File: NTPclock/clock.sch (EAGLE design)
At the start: 27 parts, among them IC1 MAX7219CNG

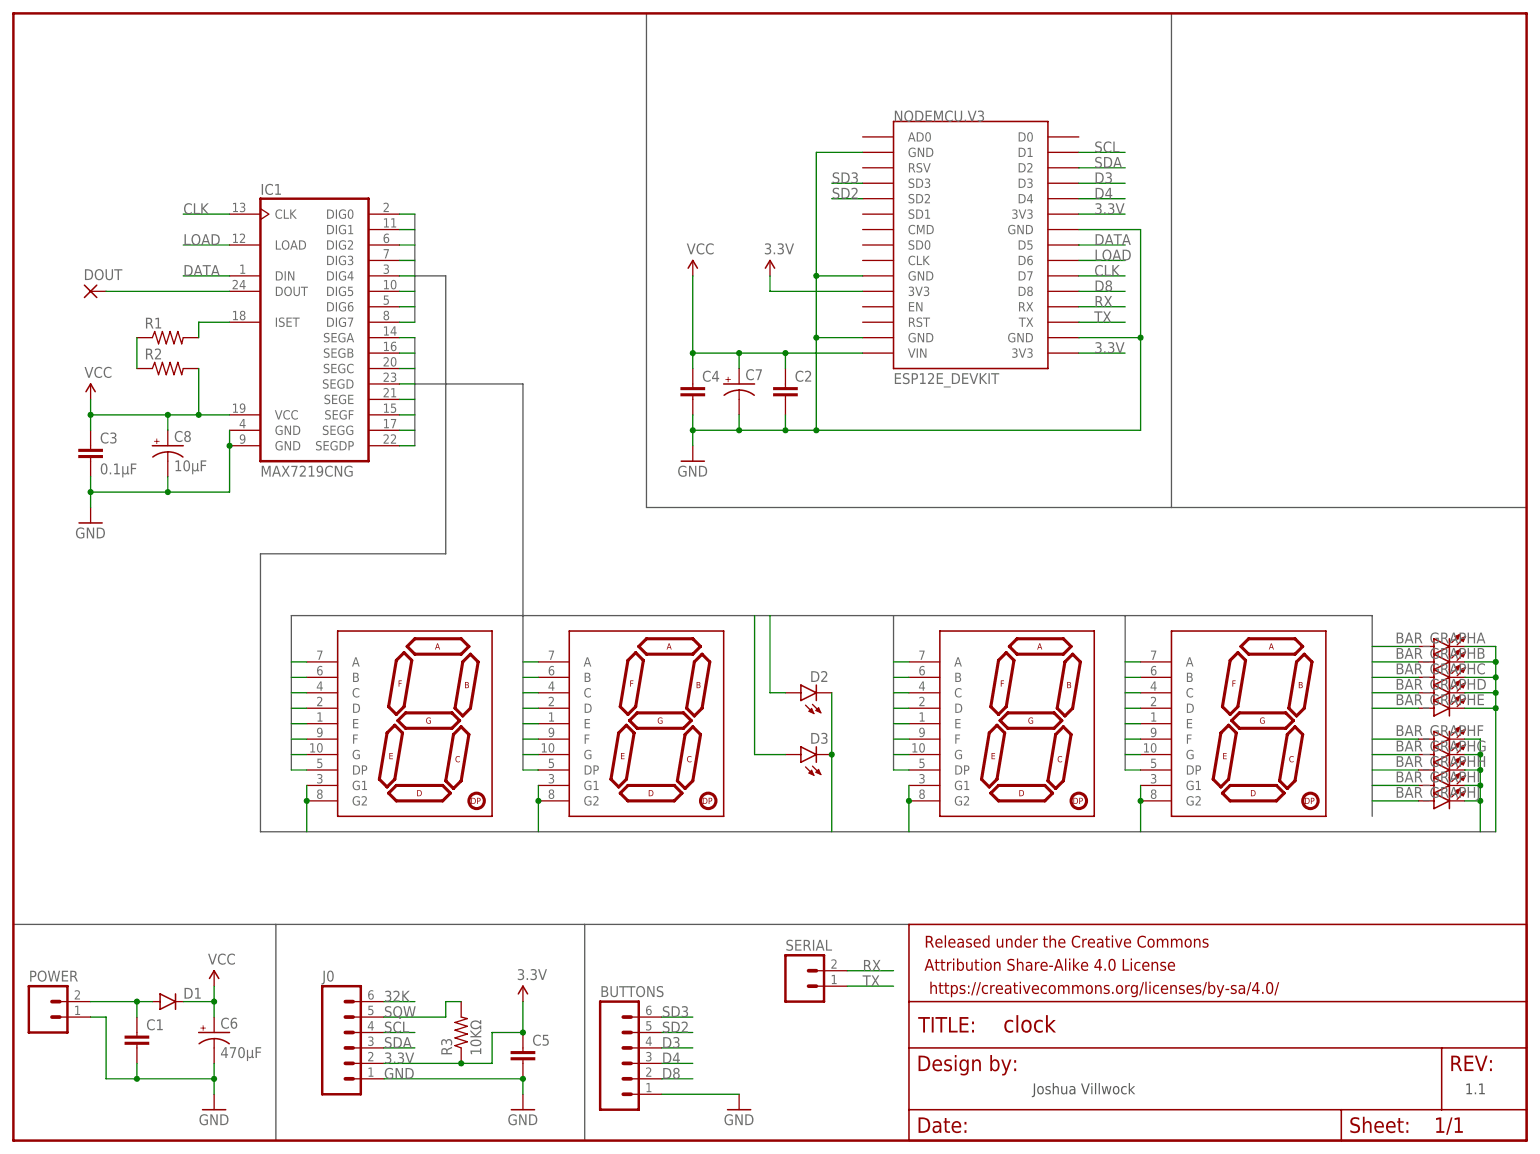
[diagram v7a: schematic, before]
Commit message: Added capacitor values
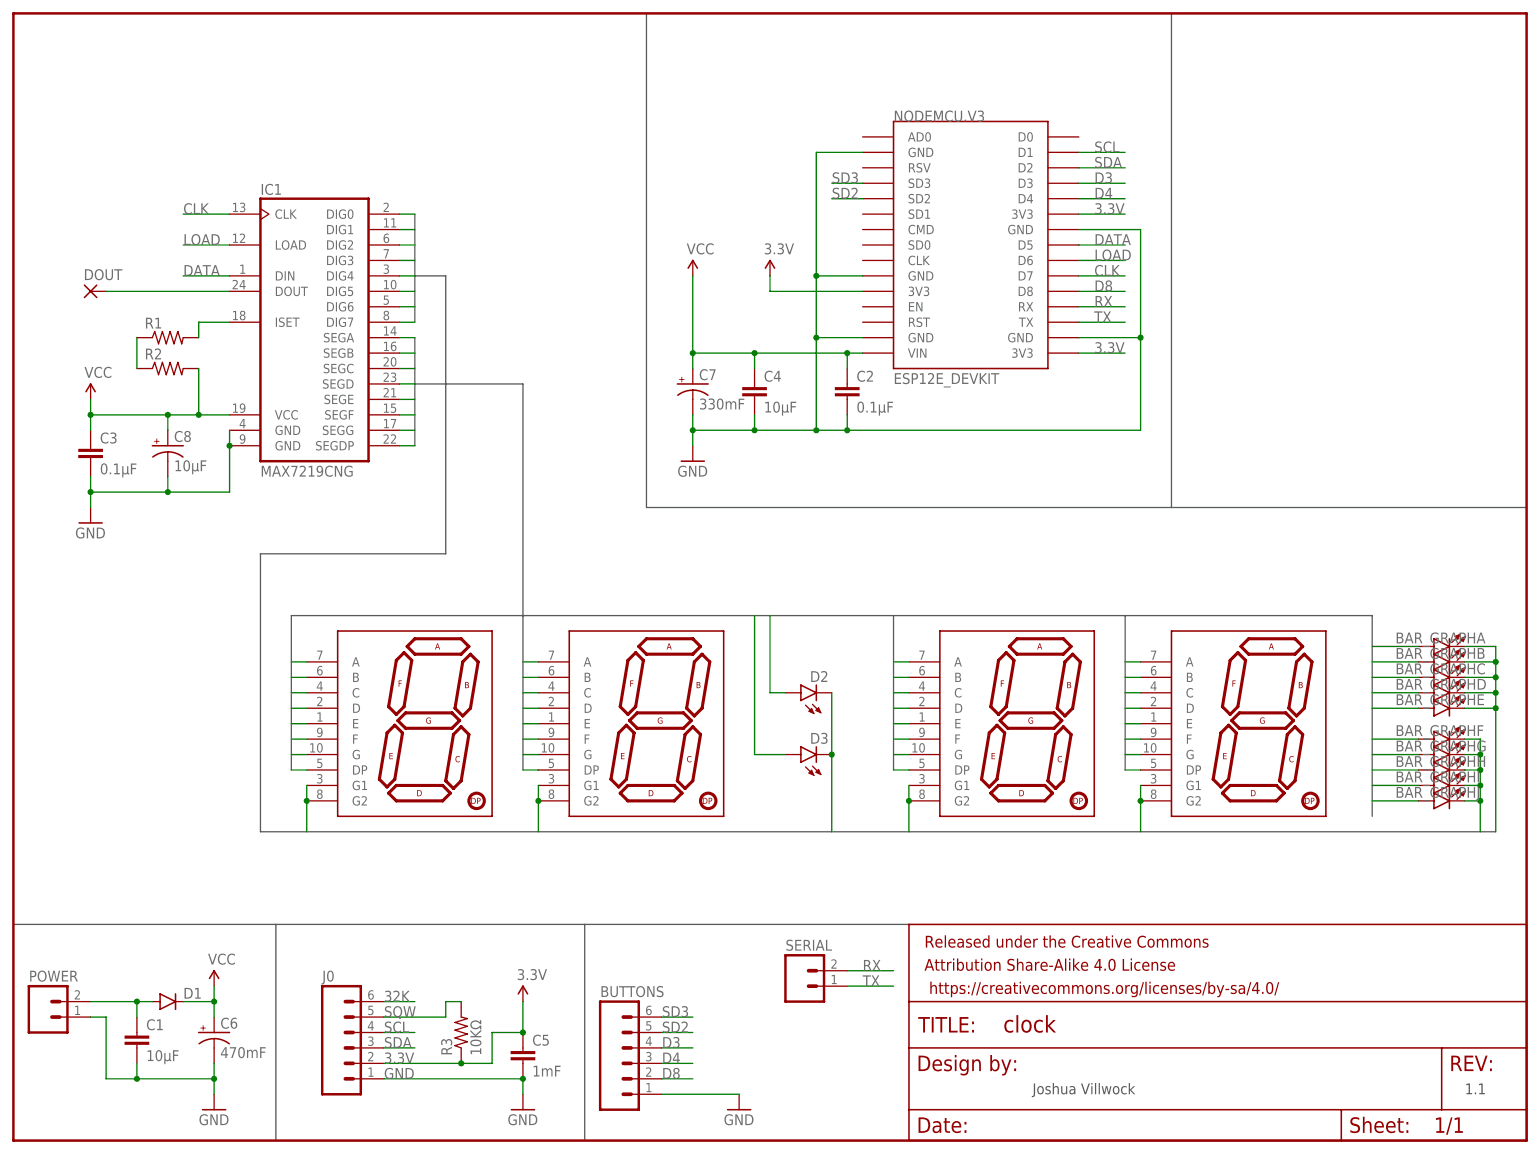
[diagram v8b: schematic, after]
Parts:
- C1, C4: value (none) -> 10μF
- C2: value (none) -> 0.1μF
- C5: value (none) -> 1mF
- C6: value 470μF -> 470mF
- C7: value (none) -> 330mF
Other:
- moved on the sheet: C2, C4, C7
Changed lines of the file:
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@@
 <part name="R1" library="SparkFun-Resistors" deviceset="RESISTOR" device="1206"/>
 <part name="R2" library="SparkFun-Resistors" deviceset="RESISTOR" device="1206"/>
-<part name="C1" library="SparkFun-Capacitors" deviceset="CAP" device="1206"/>
-<part name="C2" library="SparkFun-Capacitors" deviceset="CAP" device="1206"/>
+<part name="C1" library="SparkFun-Capacitors" deviceset="CAP" device="1206" value="10μF"/>
+<part name="C2" library="SparkFun-Capacitors" deviceset="CAP" device="1206" value="0.1μF"/>
 <part name="C3" library="SparkFun-Capacitors" deviceset="CAP" device="1206" value="0.1μF"/>
-<part name="C4" library="SparkFun-Capacitors" deviceset="CAP" device="1206"/>
-<part name="C5" library="SparkFun-Capacitors" deviceset="CAP" device="1206"/>
-<part name="C6" library="SparkFun-Capacitors" deviceset="CAP_POL" device="PTH1" value="470μF"/>
-<part name="C7" library="SparkFun-Capacitors" deviceset="CAP_POL" device="PTH1"/>
+<part name="C4" library="SparkFun-Capacitors" deviceset="CAP" device="1206" value="10μF"/>
+<part name="C5" library="SparkFun-Capacitors" deviceset="CAP" device="1206" value="1mF"/>
+<part name="C6" library="SparkFun-Capacitors" deviceset="CAP_POL" device="PTH1" value="470mF"/>
+<part name="C7" library="SparkFun-Capacitors" deviceset="CAP_POL" device="PTH1" value="330mF"/>
 <part name="C8" library="SparkFun-Capacitors" deviceset="CAP_POL" device="PTH1" value="10μF"/>
 <part name="POWER" library="SparkFun-Connectors" deviceset="M02" device="JST-PTH-VERT"/>
@@
 <instance part="R2" gate="G$1" x="50.8" y="76.2"/>
 <instance part="C1" gate="G$1" x="45.72" y="-35.56"/>
-<instance part="C2" gate="G$1" x="152.4" y="71.12"/>
+<instance part="C2" gate="G$1" x="162.56" y="71.12"/>
 <instance part="C3" gate="G$1" x="38.1" y="60.96"/>
-<instance part="C4" gate="G$1" x="137.16" y="71.12"/>
+<instance part="C4" gate="G$1" x="147.32" y="71.12"/>
 <instance part="C5" gate="G$1" x="109.22" y="-38.1"/>
 <instance part="C6" gate="G$1" x="58.42" y="-33.02"/>
-<instance part="C7" gate="G$1" x="144.78" y="73.66"/>
+<instance part="C7" gate="G$1" x="137.16" y="73.66"/>
 <instance part="C8" gate="G$1" x="50.8" y="63.5"/>
 <instance part="POWER" gate="G$1" x="30.48" y="-30.48"/>
@@
 <pinref part="C7" gate="G$1" pin="-"/>
 <pinref part="GND4" gate="1" pin="GND"/>
-<wire x1="144.78" y1="66.04" x2="137.16" y2="66.04" width="0.1524" layer="91"/>
-<wire x1="144.78" y1="66.04" x2="152.4" y2="66.04" width="0.1524" layer="91"/>
-<wire x1="152.4" y1="66.04" x2="152.4" y2="68.58" width="0.1524" layer="91"/>
-<junction x="144.78" y="66.04"/>
-<junction x="152.4" y="66.04"/>
-<wire x1="152.4" y1="66.04" x2="157.48" y2="66.04" width="0.1524" layer="91"/>
+<wire x1="147.32" y1="66.04" x2="137.16" y2="66.04" width="0.1524" layer="91"/>
+<wire x1="147.32" y1="66.04" x2="157.48" y2="66.04" width="0.1524" layer="91"/>
+<wire x1="162.56" y1="66.04" x2="162.56" y2="68.58" width="0.1524" layer="91"/>
+<junction x="162.56" y="66.04"/>
 <junction x="157.48" y="66.04"/>
-<wire x1="157.48" y1="66.04" x2="210.82" y2="66.04" width="0.1524" layer="91"/>
+<wire x1="157.48" y1="66.04" x2="162.56" y2="66.04" width="0.1524" layer="91"/>
+<wire x1="162.56" y1="66.04" x2="210.82" y2="66.04" width="0.1524" layer="91"/>
 <wire x1="137.16" y1="63.5" x2="137.16" y2="66.04" width="0.1524" layer="91"/>
 <junction x="137.16" y="66.04"/>
-<wire x1="144.78" y1="68.58" x2="144.78" y2="66.04" width="0.1524" layer="91"/>
-<wire x1="137.16" y1="66.04" x2="137.16" y2="68.58" width="0.1524" layer="91"/>
+<wire x1="147.32" y1="68.58" x2="147.32" y2="66.04" width="0.1524" layer="91"/>
+<junction x="147.32" y="66.04"/>
+<wire x1="137.16" y1="68.58" x2="137.16" y2="66.04" width="0.1524" layer="91"/>
 </segment>
 <segment>
@@
 <pinref part="C4" gate="G$1" pin="1"/>
 <pinref part="C2" gate="G$1" pin="1"/>
-<wire x1="165.1" y1="78.74" x2="152.4" y2="78.74" width="0.1524" layer="91"/>
-<wire x1="152.4" y1="78.74" x2="144.78" y2="78.74" width="0.1524" layer="91"/>
-<wire x1="144.78" y1="78.74" x2="137.16" y2="78.74" width="0.1524" layer="91"/>
-<junction x="144.78" y="78.74"/>
-<wire x1="152.4" y1="76.2" x2="152.4" y2="78.74" width="0.1524" layer="91"/>
-<junction x="152.4" y="78.74"/>
+<wire x1="165.1" y1="78.74" x2="162.56" y2="78.74" width="0.1524" layer="91"/>
+<wire x1="162.56" y1="78.74" x2="147.32" y2="78.74" width="0.1524" layer="91"/>
+<wire x1="147.32" y1="78.74" x2="137.16" y2="78.74" width="0.1524" layer="91"/>
+<wire x1="162.56" y1="76.2" x2="162.56" y2="78.74" width="0.1524" layer="91"/>
+<junction x="162.56" y="78.74"/>
 <junction x="137.16" y="78.74"/>
-<wire x1="144.78" y1="78.74" x2="144.78" y2="76.2" width="0.1524" layer="91"/>
-<wire x1="137.16" y1="76.2" x2="137.16" y2="78.74" width="0.1524" layer="91"/>
+<wire x1="137.16" y1="78.74" x2="137.16" y2="76.2" width="0.1524" layer="91"/>
+<wire x1="147.32" y1="76.2" x2="147.32" y2="78.74" width="0.1524" layer="91"/>
+<junction x="147.32" y="78.74"/>
 </segment>
 <segment>
@@
 </sheet>
 </sheets>
+<errors>
+</errors>
 </schematic>
 </drawing>
